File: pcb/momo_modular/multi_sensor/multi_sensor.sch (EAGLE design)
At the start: 28 parts, among them U1 AP7115-LDO, U2 16LF1847, U3 TS1100

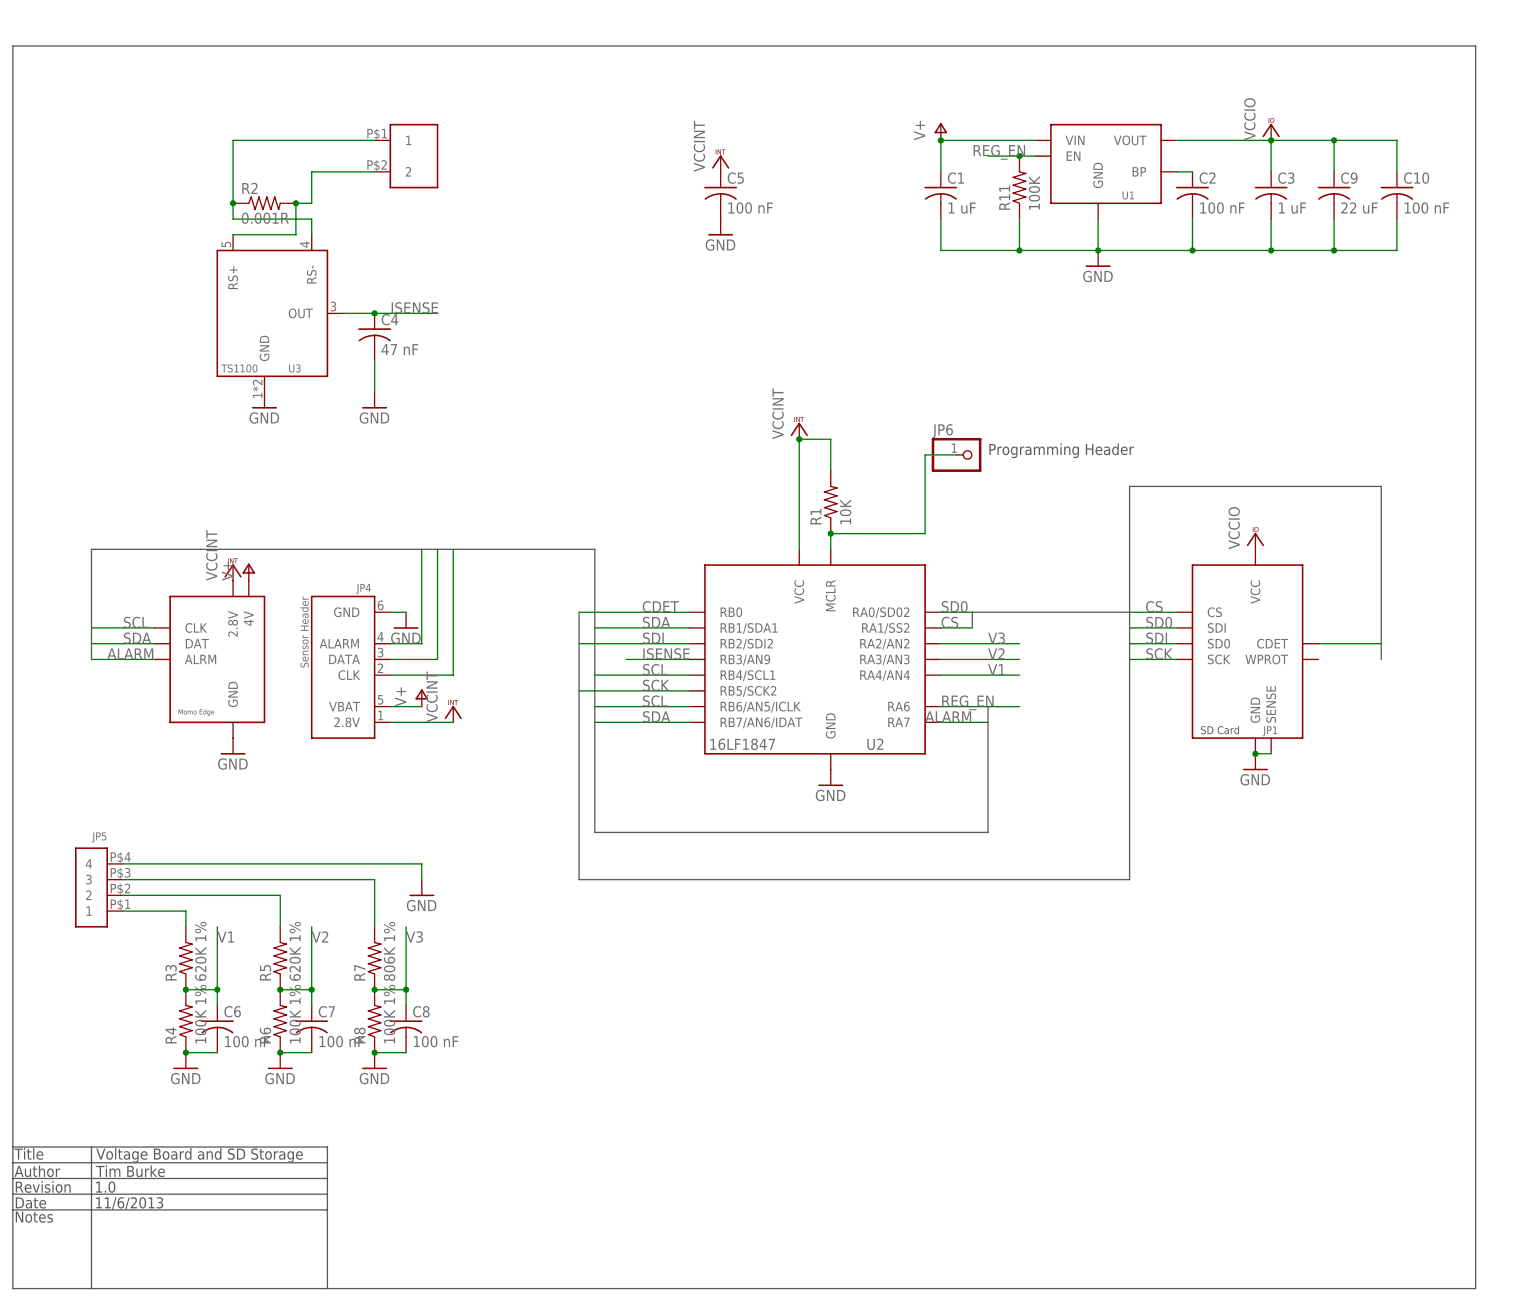
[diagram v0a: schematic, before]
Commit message: Finish v1 of multi_sensor board
Board is based on the elec_sensor_sd board previously made but with
the following changes:
- removed SD card b/c of space
- added sensors
	+ pulse counting (turbine flow sensor)
	+ 3 voltages from 0-30V
	+ 1 current from 0-15A
	+ external serial connection bidirectional and 5V tolerant
	+ wheatstone bridge sensor connection
	+ differential analog voltage
	+ pressure sensor (SM5470 for venturi sensing)

All of the analog sensors are built around a digitally controllable
instrumentation amplifier AD8557.  It's a pricey part but should
give us a lot of flexibility for retargeting the board in the future
and it lets us avoid needing to do lots of calibration.

Other key feature is that all of the analog sensors can automatically
have their input offset voltage nulled out because 2 muxes let you
switch the input polarity of any input.  The signal will then change
sign but the offset will not, so you can determine the offset voltage
without manual calibration.  The AD8557 can be reprogrammed in the
field to change its gain and output offset to compensate.
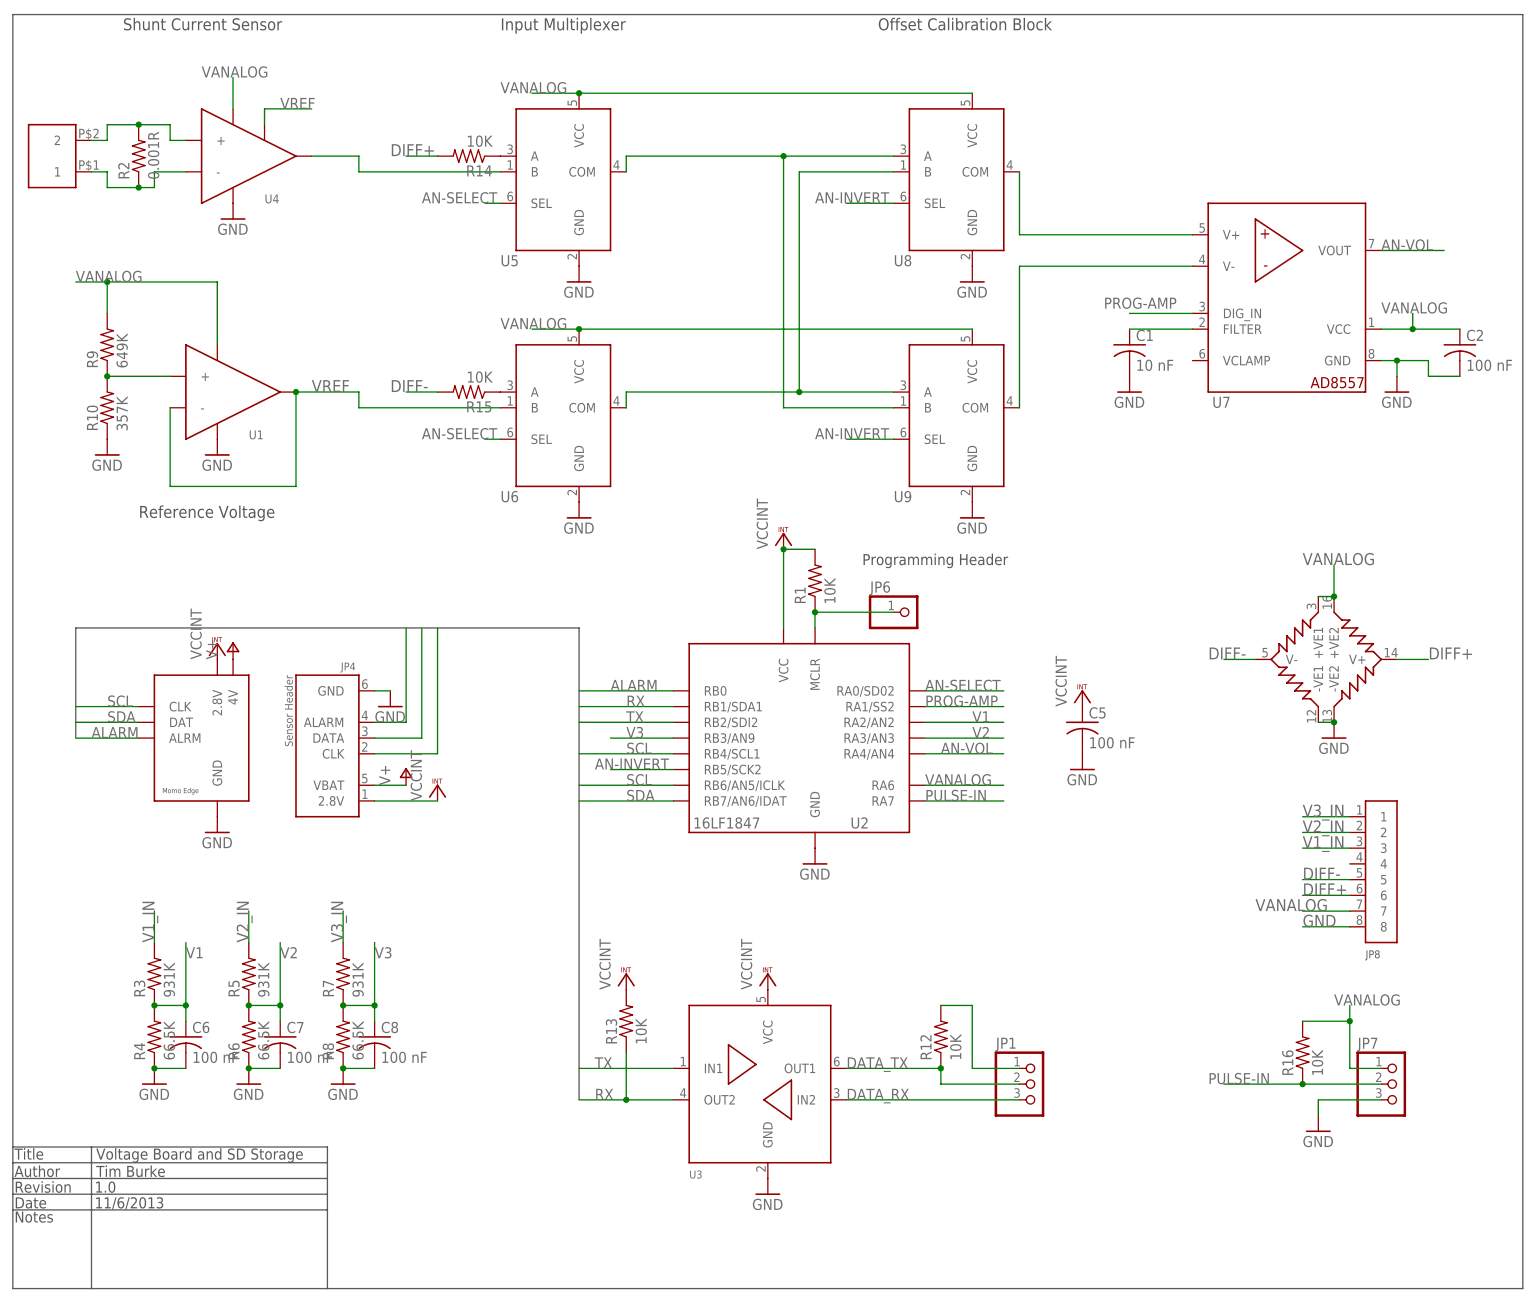
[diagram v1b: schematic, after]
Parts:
- removed C10: 100 nF, rcl:C-USC0402K
- removed C3: 1 uF, rcl:C-USC0402K
- removed C4: 47 nF, rcl:C-USC0402K
- removed C9: 22 uF, rcl:C-USC1206K
- removed JP5: SCREWTERM4, components:SCREWTERM4
- removed R11: 100K, rcl:R-US_R0603
- added JP7: (no value), pinhead:PINHD-1X3
- added JP8: 8PIN-TERMBLOCK-PUSH, components:8PIN-TERMBLOCK-PUSH
- added R10: 357K, rcl:R-US_R0603
- added R12, R13, R14, R15, R16: 10K, rcl:R-US_R0603
- added R9: 649K, rcl:R-US_R0603
- added U10: SM5470-DIFF-PRESS-SENSOR, components:SM5470-DIFF-PRESS-SENSOR
- added U4: LT1990, components:LT1990
- added U5, U6, U8, U9: 2:1-MUX, components:2:1-MUX
- added U7: AD8557-DIGITRIM-OPAMP, components:AD8557-DIGITRIM-OPAMP
- C1: value 1 uF -> 10 nF; device rcl:C-USC0402K -> rcl:C-USC0402; DIGIKEY-PN 445-4114-1-ND -> 490-6286-1-ND
- JP1: value SDCARD-HOLDER -> (none); device components:SDCARD-HOLDER -> pinhead:PINHD-1X3
- R3, R5: value 620K 1% -> 931K; DIGIKEY-PN P620KHCT-ND -> RHM931KCLCT-ND
- R4, R6, R8: value 100K 1% -> 66.5K; DIGIKEY-PN P100KHCT-ND -> RC0603FR-0766K5L
- R7: value 806K 1% -> 931K; DIGIKEY-PN P806KHCT-ND -> RHM931KCLCT-ND
- U1: value AP7115-LDO -> MCP6001U; device components:AP7115-LDO -> components:MCP6001U
- U3: value TS1100 -> DUAL-BUFFER-OD-NC7WZ07; device components:TS1100 -> components:DUAL-BUFFER-OD-NC7WZ07
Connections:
- removed net CDET: JP1.CDET, U2.RB0
- removed net CS: JP1.CS, U2.RA1/SS2
- removed net ISENSE: C4.1, U2.RB3/AN9, U3.OUT
- removed net N$10: JP5.1, R3.2
- removed net N$11: JP5.2, R5.2
- removed net N$12: JP5.3, R7.2
- removed net REG_EN: R11.2, U1.EN, U2.RA6
- removed net SCK: JP1.SCK, U2.RB5/SCK2
- removed net SD0: JP1.SDI, U2.RA0/SD02
- removed net SDI: JP1.SD0, U2.RB2/SDI2
- removed net VCCIO: C10.1, C3.1, C9.1, JP1.VCC, U1.VOUT
- new net AN-INVERT: U2.RB5/SCK2, U8.SEL, U9.SEL
- new net AN-SELECT: U2.RA0/SD02, U5.SEL, U6.SEL
- new net AN-VOL: U2.RA4/AN4, U7.VOUT
- new net DATA_RX: JP1.3, U3.IN2
- new net DATA_TX: JP1.2, R12.1, U3.OUT1
- new net DIFF+: JP8.6, R14.2, U10.V+
- new net DIFF-: JP8.5, R15.2, U10.V-
- new net N$13: U7.V+, U8.COM
- new net N$14: U7.V-, U9.COM
- new net N$16: U4.OUT, U5.B
- new net N$2: JP1.1, R12.2
- new net N$5: U5.COM, U8.A, U9.B
- new net N$6: R14.1, U5.A
- new net N$7: C1.1, U7.FILTER
- new net N$8: U6.COM, U8.B, U9.A
- new net N$9: R15.1, U6.A
- new net PROG-AMP: U2.RA1/SS2, U7.DIG_IN
- new net PULSE-IN: JP7.2, R16.1, U2.RA7
- new net RX: R13.1, U2.RB1/SDA1, U3.OUT2
- new net TX: U2.RB2/SDI2, U3.IN1
- new net V1_IN: JP8.3, R3.2
- new net V2_IN: JP8.2, R5.2
- new net V3_IN: JP8.1, R7.2
- new net VANALOG: C2.1, JP7.1, JP8.7, R16.2, R9.2, U1.VCC, U10.+VE1, U10.+VE2, U2.RA6, U4.VCC, U5.VCC, U6.VCC, U7.VCC, U8.VCC, U9.VCC
- new net VREF: U1.-, U1.OUT, U4.SHUT, U6.B
- net ALARM: now also U2.RB0; no longer U2.RA7
- net GND: now also JP7.3, JP8.8, R10.1, U10.-VE1, U10.-VE2, U4.GND, U5.GND, U6.GND, U7.GND, U8.GND, U9.GND; no longer C10.2, C3.2, C4.2, C9.2, JP1.GND, JP1.SENSE, JP5.4, R11.1
- net N$3: now also R10.2, R9.1, U1.+; no longer C2.1, U1.BP
- net RS+: now also JP3.1, R2.1, U4.-; no longer JP3.2, R2.2, U3.RS+
- net RS-: now also JP3.2, R2.2, U4.+; no longer JP3.1, R2.1, U3.RS-
- net SDA: no longer U2.RB1/SDA1
- net V+: no longer C1.1, U1.VIN
- net V1: now also U2.RA2/AN2; no longer U2.RA4/AN4
- net V3: now also U2.RB3/AN9; no longer U2.RA2/AN2
- net VCCINT: now also R13.2, U3.VCC
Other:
- note added: "Input Multiplexer"
- note added: "Offset Calibration Block"
- note added: "Reference Voltage"
- note added: "Shunt Current Sensor"
- moved on the sheet: C1, C2, C5, C6, C7, C8, JP4, JP6, R1, R2, R3, R4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

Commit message: Final layout touches
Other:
- note added: "3/30/2014"
- note added: "Multisensor Acquisition Board"
- note removed: "11/6/2013"
- note removed: "Voltage Board and SD Storage"
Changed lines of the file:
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@@
 <text x="-116.586" y="-96.266" size="1.778" layer="97">Date</text>
 <text x="-116.586" y="-98.552" size="1.778" layer="97">Notes</text>
-<text x="-103.378" y="-88.392" size="1.778" layer="97">Voltage Board and SD Storage</text>
+<text x="-103.378" y="-88.392" size="1.778" layer="97">Multisensor Acquisition Board</text>
 <text x="-103.378" y="-91.186" size="1.778" layer="97">Tim Burke</text>
 <text x="-103.632" y="-93.726" size="1.778" layer="97">1.0</text>
-<text x="-103.632" y="-96.266" size="1.778" layer="97">11/6/2013</text>
+<text x="-103.632" y="-96.266" size="1.778" layer="97">3/30/2014</text>
 <text x="20.32" y="7.62" size="1.778" layer="97">Programming Header</text>
 <text x="22.86" y="93.98" size="1.9304" layer="97">Offset Calibration Block</text>

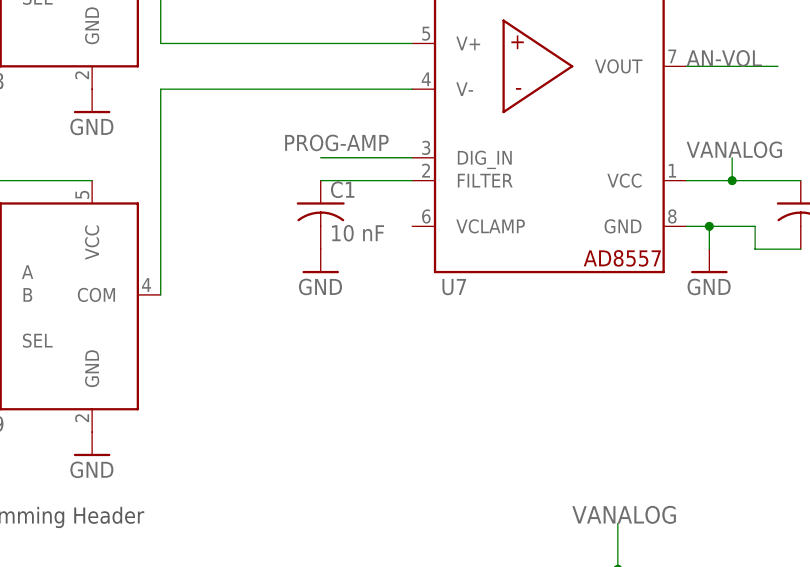
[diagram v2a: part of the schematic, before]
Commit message: Connect Vclamp and Vdd on in-amp
Vclamp is specified to not be floating even when not in use.
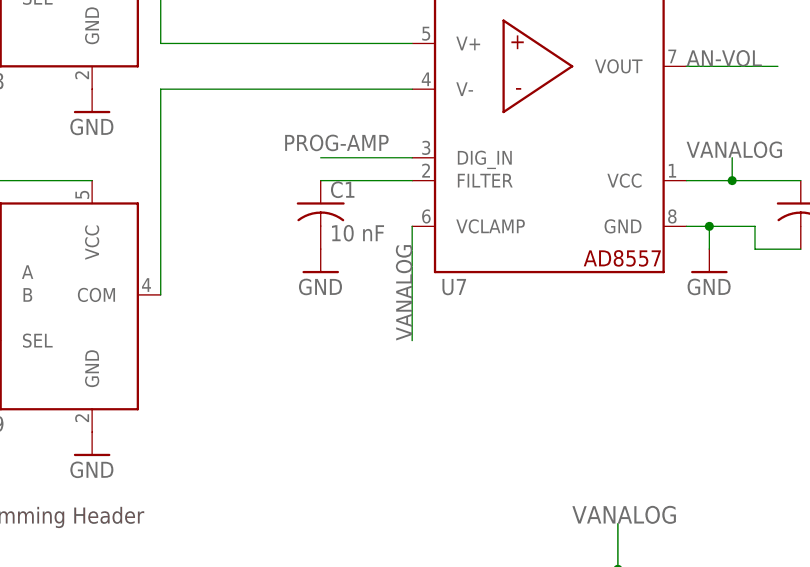
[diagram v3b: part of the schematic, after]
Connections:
- net VANALOG: now also U7.VCLAMP
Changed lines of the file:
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@@
 <label x="83.82" y="-48.26" size="1.9304" layer="95"/>
+</segment>
+<segment>
+<pinref part="U7" gate="G$1" pin="VCLAMP"/>
+<wire x1="73.66" y1="40.64" x2="73.66" y2="27.94" width="0.1524" layer="91"/>
+<label x="73.66" y="27.94" size="1.778" layer="95" rot="R90"/>
 </segment>
 </net>
